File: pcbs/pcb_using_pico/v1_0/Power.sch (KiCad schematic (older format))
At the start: 22 parts, among them J3 Barrel_Jack, J4 Connector_USB_B_Micro, U6 AMS1117-3.3, U7 AMS1117-5.0, U8 ETA6002

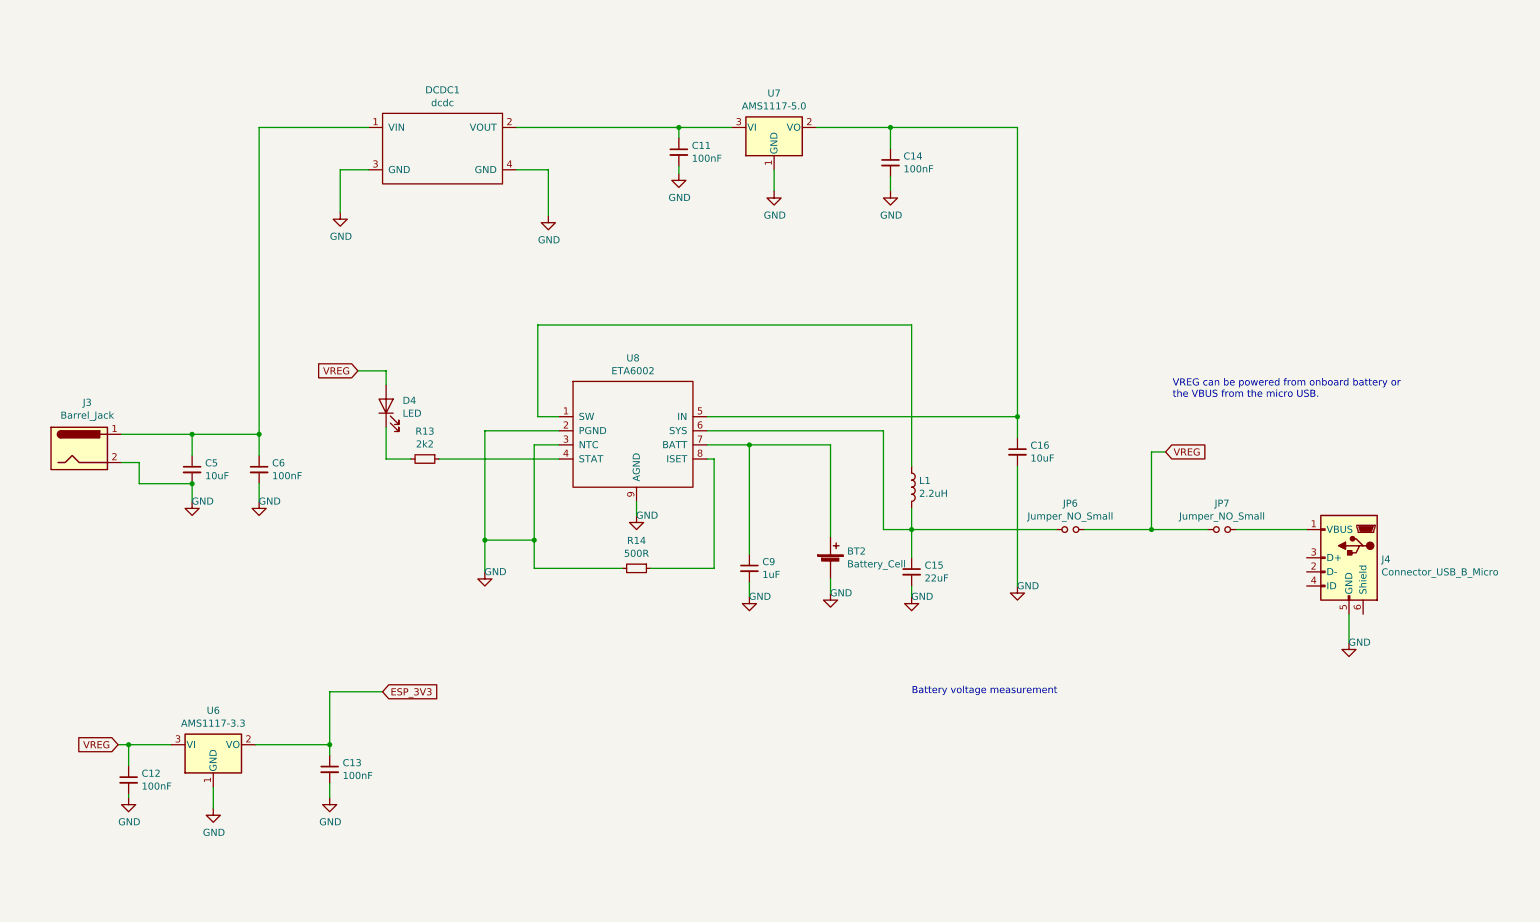
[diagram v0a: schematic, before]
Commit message: V2.0 sent off for fab. New charger IC with more solderable footprint, plus other fixes
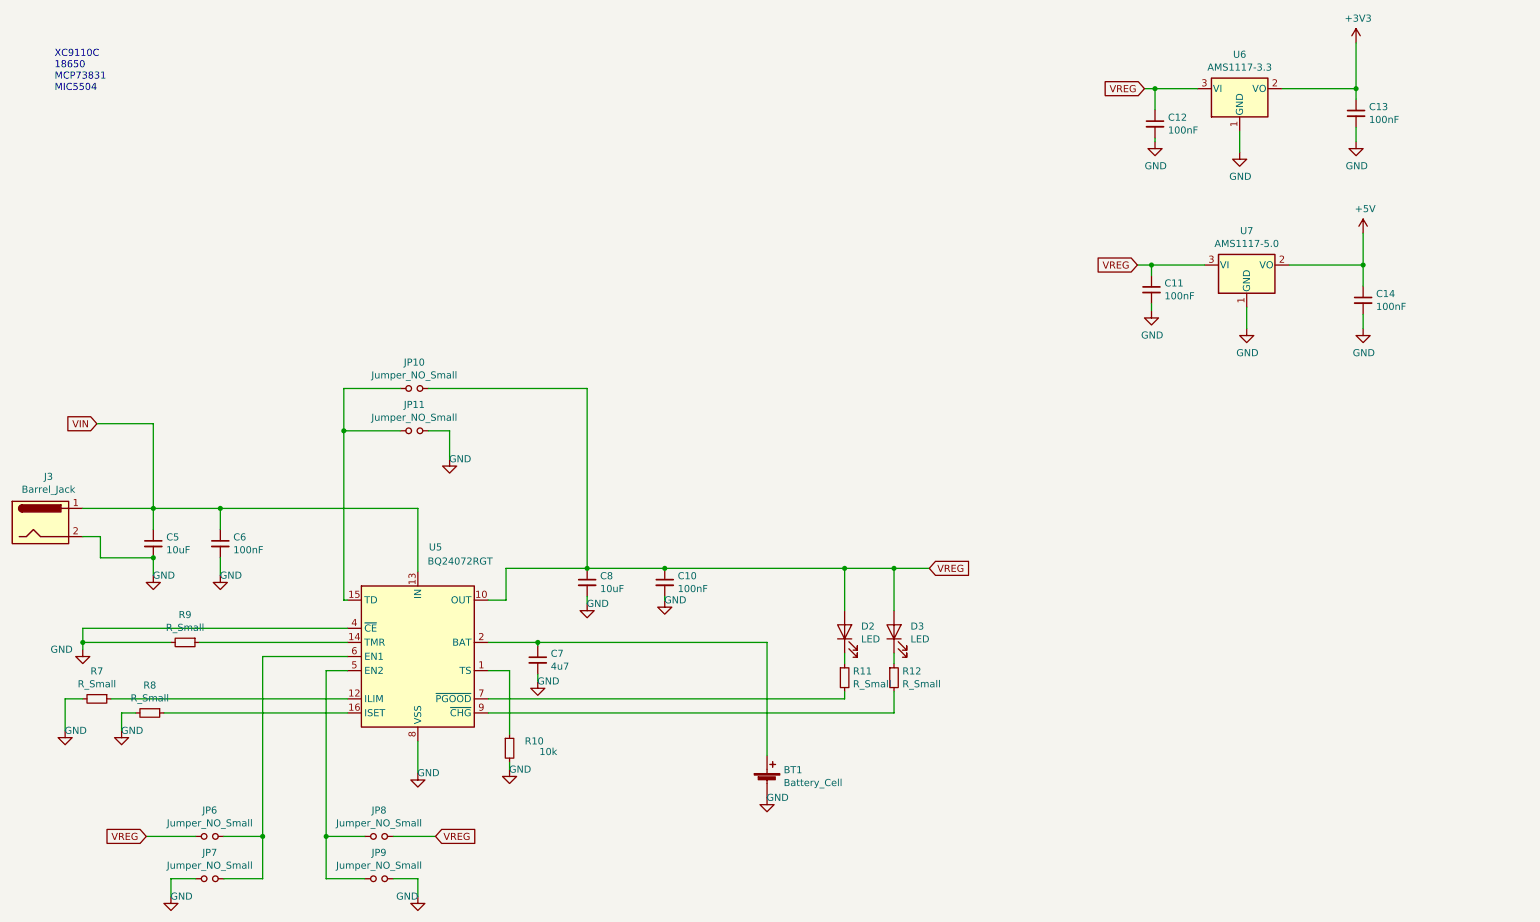
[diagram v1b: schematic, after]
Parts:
- removed BT2: Battery_Cell, Battery:BatteryHolder_Keystone_1042_1x18650, symbol Device:Battery_Cell
- removed C15: 22uF, Capacitor_SMD:C_1206_3216Metric_Pad1.42x1.75mm_HandSolder, symbol Device:C_Small
- removed C16: 10uF, Capacitor_SMD:C_1206_3216Metric_Pad1.42x1.75mm_HandSolder, symbol Device:C_Small
- removed C9: 1uF, Capacitor_SMD:C_1206_3216Metric_Pad1.42x1.75mm_HandSolder, symbol Device:C_Small
- removed D4: LED, LED_SMD:LED_0805_2012Metric_Pad1.15x1.40mm_HandSolder, symbol Device:LED
- removed DCDC1: dcdc, Connector_PinHeader_2.54mm:PinHeader_1x04_P2.54mm_Vertical, symbol New_Library:dcdc
- removed J4: Connector_USB_B_Micro, Connector_USB:USB_Micro-B_GCT_USB3076-30-A, symbol cq1re1-cache:Connector_USB_B_Micro
- removed L1: 2.2uH, Inductor_SMD:L_Coilcraft_LPS5030, symbol Device:L
- removed R13: 2k2, Resistor_SMD:R_0805_2012Metric, symbol Device:R_Small
- removed R14: 500R, Resistor_SMD:R_0805_2012Metric, symbol Device:R_Small
- removed U8: ETA6002, Package_SO:SOIC-8-1EP_3.9x4.9mm_P1.27mm_EP2.514x3.2mm, symbol pak_breakout:ETA6002
- added BT1: Battery_Cell, Battery:BatteryHolder_Keystone_1042_1x18650, symbol Device:Battery_Cell
- added C10: 100nF, Capacitor_SMD:C_0805_2012Metric, symbol Device:C_Small
- added C7: 4u7, Capacitor_SMD:C_1206_3216Metric_Pad1.42x1.75mm_HandSolder, symbol Device:C_Small
- added C8: 10uF, Capacitor_SMD:C_1206_3216Metric_Pad1.42x1.75mm_HandSolder, symbol Device:C_Small
- added D2, D3: LED, LED_SMD:LED_0805_2012Metric_Pad1.15x1.40mm_HandSolder, symbol Device:LED
- added JP10, JP11, JP8, JP9: Jumper_NO_Small, Jumper:SolderJumper-2_P1.3mm_Open_RoundedPad1.0x1.5mm, symbol Device:Jumper_NO_Small
- added R10: 10k, Resistor_SMD:R_0805_2012Metric, symbol Device:R_Small
- added R11, R12, R7, R8, R9: R_Small, Resistor_SMD:R_0805_2012Metric, symbol Device:R_Small
- added U5: BQ24072RGT, Package_DFN_QFN:VQFN-16-1EP_3x3mm_P0.5mm_EP1.6x1.6mm, symbol Battery_Management:BQ24072RGT
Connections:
- net GND: now also JP7.1, BT1.2 (-), C10.2, C7.2, C8.2, JP11.2, JP9.1, R10.2, R7.2, R8.2, R9.2, U5.17 (VSS), U5.4 (~CE), U5.8 (VSS)
- net VREG: now also C11.1, U7.3 (VI), C10.1, C8.1, D2.2 (A), D3.2 (A), JP10.2, JP8.1, U5.10 (OUT), U5.11 (OUT); no longer JP7.1
- net +5V: now reaches C14.1, U7.2 (VO)
- net VIN: now reaches C5.1, C6.1, J3.1
- net VIN: now also U5.13 (IN)
- net at JP6.2: now also JP7.2, U5.6 (EN1)
- net ESP_3V3 renamed +3V3
- new net: R10.1, U5.1 (TS)
- new net: R7.1, U5.12 (ILIM)
- new net: R9.1, U5.14 (TMR)
- new net: JP10.1, JP11.1, U5.15 (TD)
- new net: R8.1, U5.16 (ISET)
- new net: BT1.1 (+), C7.1, U5.2 (BAT), U5.3 (BAT)
- new net: JP8.2, JP9.2, U5.5 (EN2)
- new net: R11.2, U5.7 (~PGOOD)
- new net: R12.2, U5.9 (~CHG)
- new net: D2.1 (K), R11.1
- new net: D3.1 (K), R12.1
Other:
- note added: "XC9110C\n18650\nMCP73831\nMIC5504\n"
- note removed: "Battery voltage measurement\n"
- note removed: "VREG can be powered from onboard battery or\nthe VBUS from the micro USB."
- moved on the sheet: C11, C12, C13, C14, C5, C6, J3, U6, U7
